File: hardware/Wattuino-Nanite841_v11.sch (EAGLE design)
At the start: 20 parts, among them IC1 ATTINY841-MU, J1 USB-MICROB-2, J2 MA07-1, J3 MA07-1, SW1 SW-TACTILE-PTS840P, X1 PASSER-07, X2 PASSER-07, X3 PASSER-07

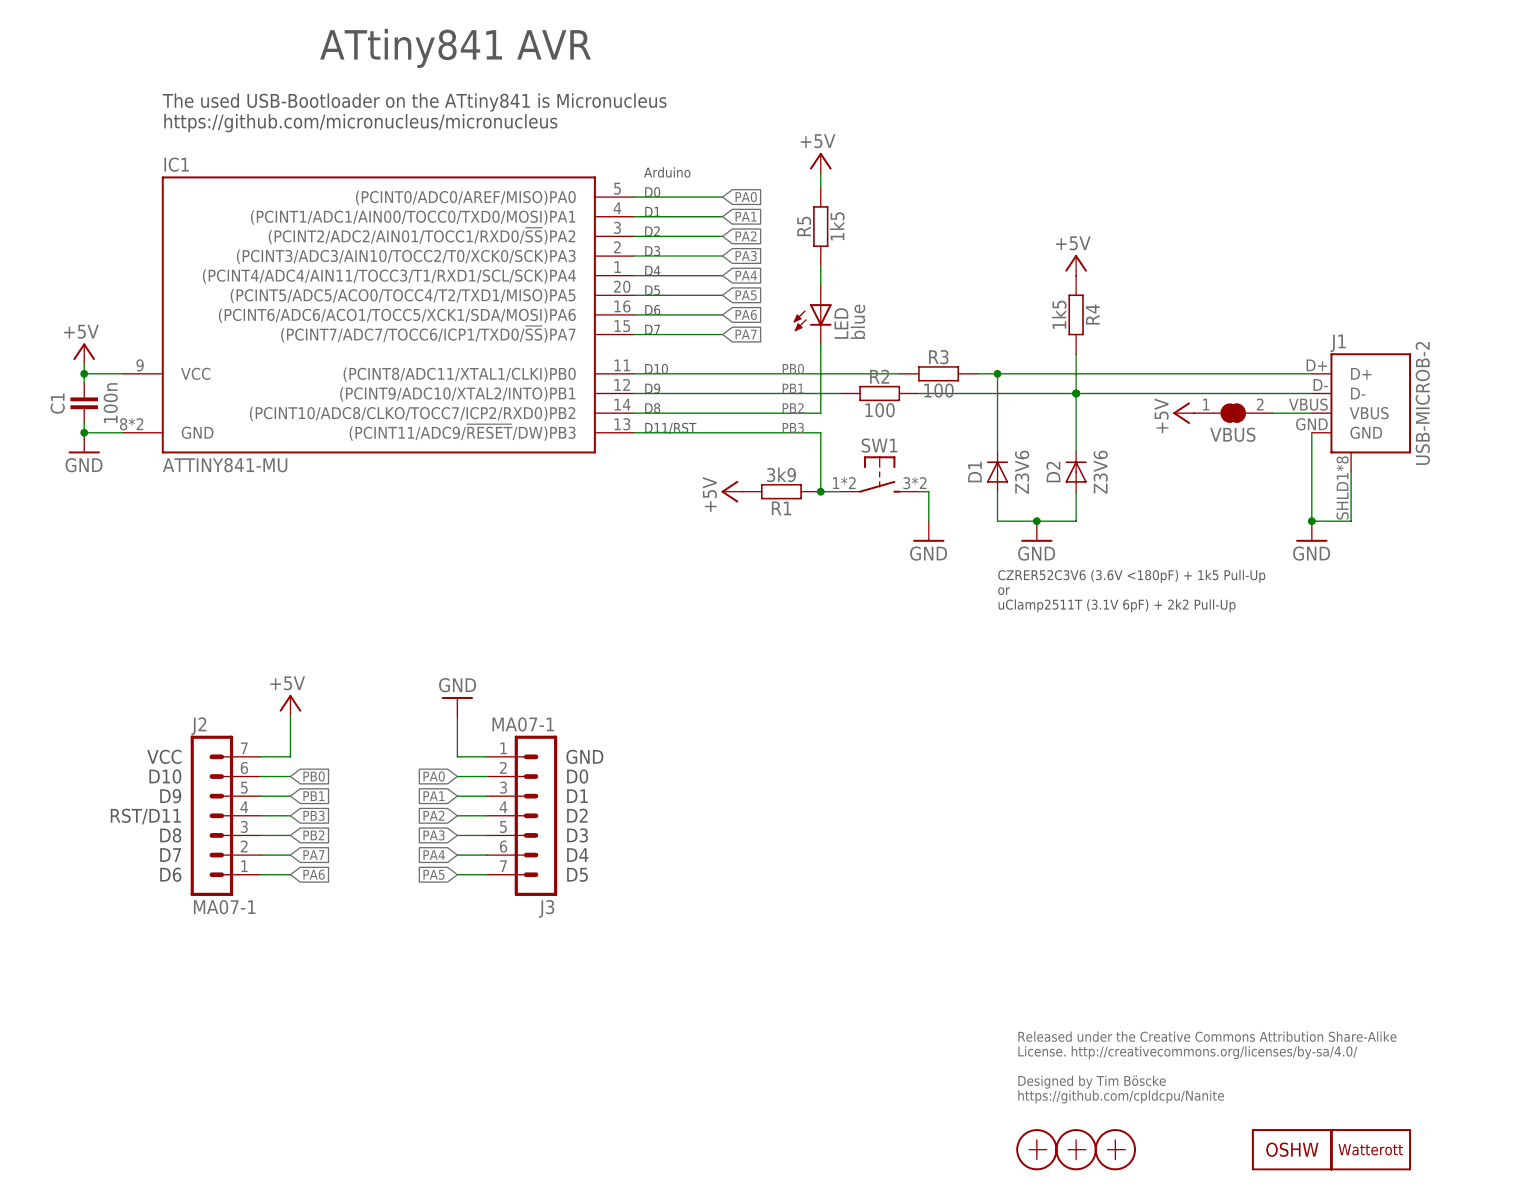
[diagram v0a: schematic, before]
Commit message: updated schematics
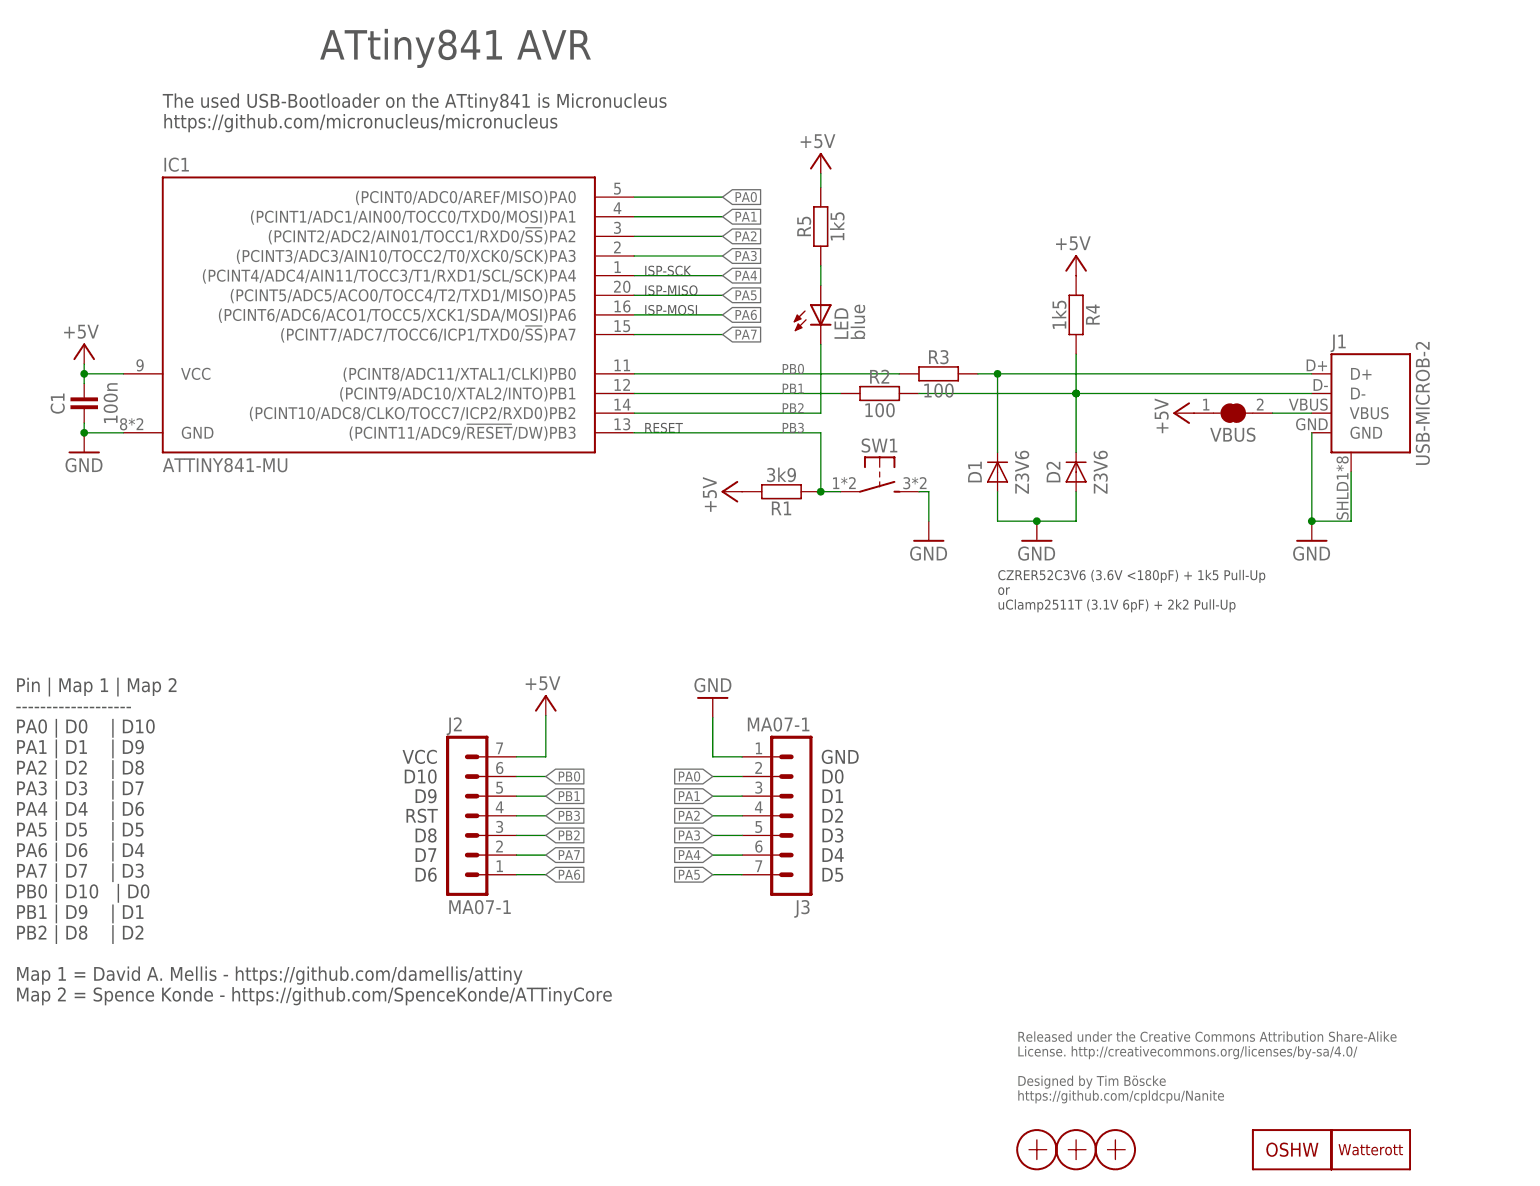
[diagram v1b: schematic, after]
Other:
- note added: "ISP-MISO"
- note added: "ISP-MOSI"
- note added: "ISP-SCK"
- note added: "Pin | Map 1 | Map 2 ------------------- PA0 | D0 | D10 PA1 | D1 | D9 PA2 | D2 | D8 PA3 | D3 | D7 PA4 | D4 | D6 PA5 | D5 | D5 PA6 | D6 | D4 PA7 | D7 | D3 PB0 | D10 | D0 PB1 | D9 | D1 PB2 | D8 | D2 Map 1 = David A. Mellis - https://github.com/damellis/attiny Map 2 = Spence Konde - https://github.com/SpenceKonde/ATTinyCore"
- note added: "RESET"
- note added: "RST"
- note removed: "Arduino"
- note removed: "D11/RST"
- note removed: "RST/D11"
- moved on the sheet: J2, J3
